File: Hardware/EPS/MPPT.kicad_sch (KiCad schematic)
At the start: 27 parts, among them J301 Conn_02x02_Counter_Clockwise, Q301 RQ3G100GNTB, Q302 RQ3G100GNTB, U301 LTC4162EUFD-L41#PBF

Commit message: Finished EPS - v0.1.0
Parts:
- C301, C303: value 0.1uF -> 100nF
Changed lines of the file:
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@@
   (title_block
     (title "EPS Schematics")
-    (date "2023-04-08")
-    (rev "v0.0.3")
-    (comment 1 "e-mail: ")
+    (date "2023-04-19")
+    (rev "v0.1.0")
+    (comment 1 "LinkedIn: linkedin.com/in/carlos-martinez-mora-7b2023230/")
     (comment 2 "Author: Carlos Martinez Mora")
   )
@@
     (in_bom yes) (on_board yes)
     (property "Reference" "C301" (id 0) (at 107.95 57.15 0))
-    (property "Value" "0.1uF" (id 1) (at 107.95 59.69 0))
+    (property "Value" "100nF" (id 1) (at 107.95 59.69 0))
     (property "Footprint" "Capacitor_SMD:C_0603_1608Metric_Pad1.08x0.95mm_HandSolder" (id 2) (at 113.9952 62.23 0)
       (effects (font (size 1.27 1.27)) hide)
@@
     (in_bom yes) (on_board yes)
     (property "Reference" "C303" (id 0) (at 168.91 58.42 90))
-    (property "Value" "0.1uF" (id 1) (at 168.91 60.96 90))
+    (property "Value" "100nF" (id 1) (at 168.91 60.96 90))
     (property "Footprint" "Capacitor_SMD:C_0603_1608Metric_Pad1.08x0.95mm_HandSolder" (id 2) (at 172.72 63.8048 0)
       (effects (font (size 1.27 1.27)) hide)

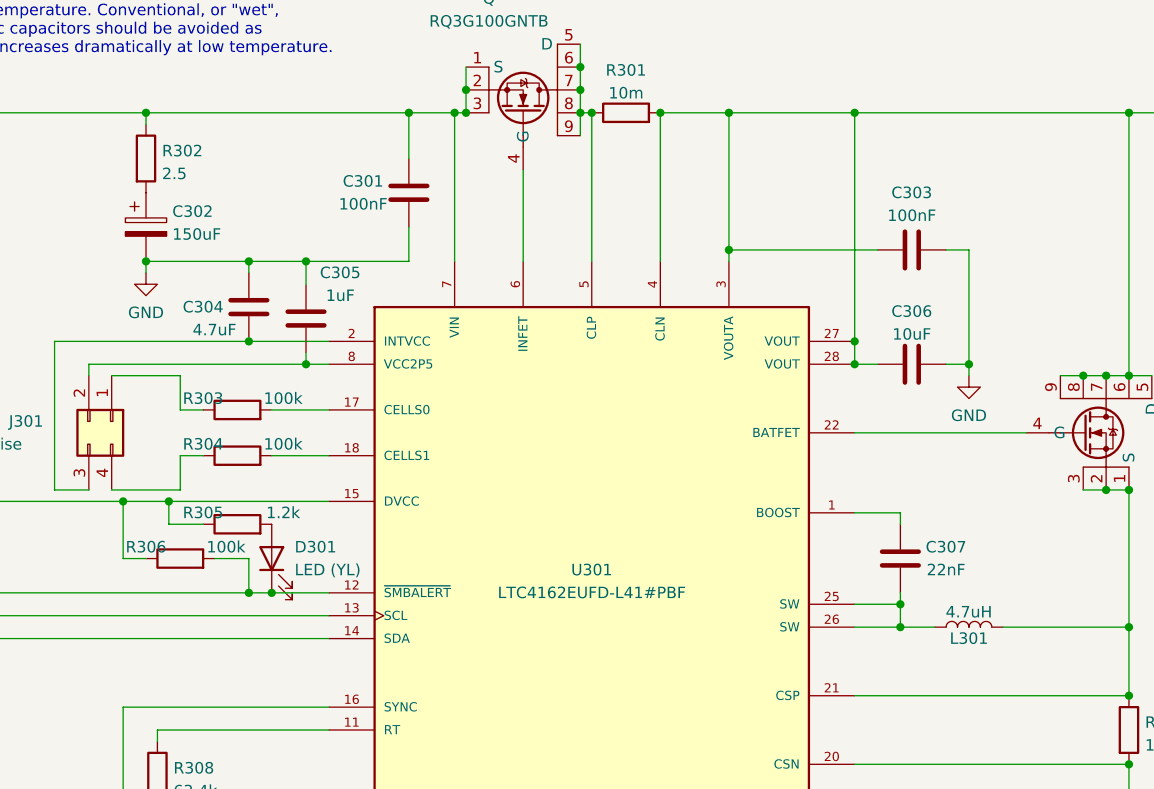
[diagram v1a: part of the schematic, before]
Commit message: Updated to KiCAD 7.0
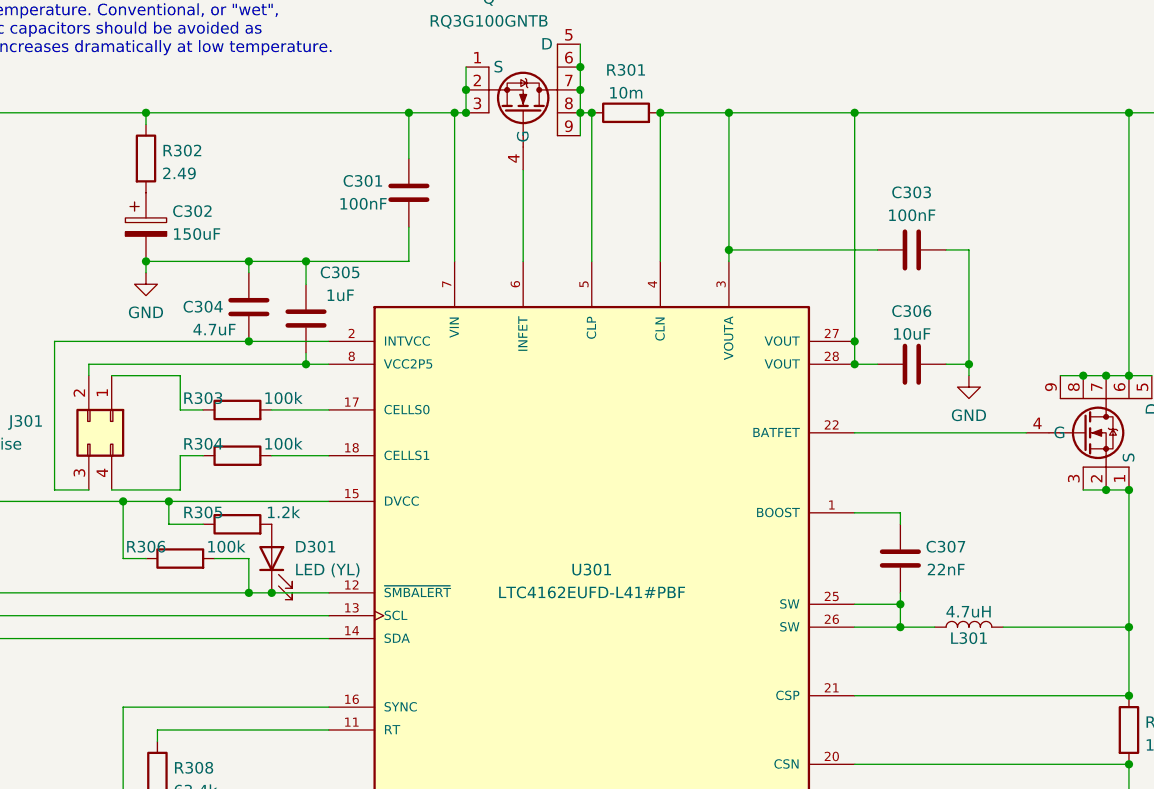
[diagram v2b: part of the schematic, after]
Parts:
- R302: value 2.5 -> 2.49; footprint Resistor_SMD:R_0603_1608Metric_Pad0.98x0.95mm_HandSolder -> Resistor_SMD:R_1206_3216Metric_Pad1.30x1.75mm_HandSolder
- TH301: footprint Resistor_SMD:R_0603_1608Metric_Pad0.98x0.95mm_HandSolder -> Connector_PinHeader_1.00mm:PinHeader_1x02_P1.00mm_Vertical
